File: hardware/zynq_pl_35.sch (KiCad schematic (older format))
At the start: 1 part

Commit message: Added a few Todos.
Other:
- note added: "TODO: VCCO(AFAIK 1,8 V), is VREF needed for this single ended signals?"
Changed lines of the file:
@@
 Wire Wire Line
 	5050 2400 5400 2400
+Text Notes 1000 850  0    60   ~ 0
+TODO: VCCO(AFAIK 1,8 V), is VREF needed for this single ended signals?
 $EndSCHEMATC

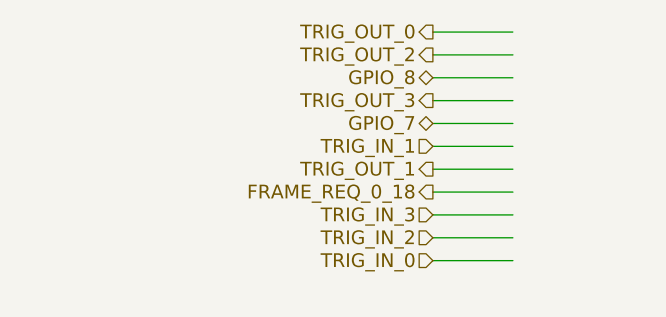
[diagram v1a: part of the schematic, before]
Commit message: Added decoupling Capacitors for the Zynq. Also added the 2,5 V Power supply.
The 2,5 V supply was implemented as LDO and is sourced by the 3,3 V Line.
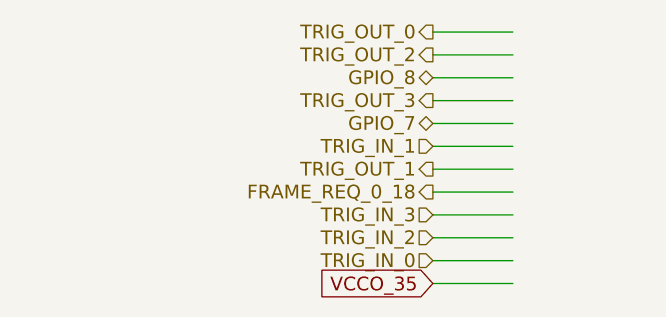
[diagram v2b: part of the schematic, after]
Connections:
- net labels added: VCCO_35
- wire segments 41 -> 42
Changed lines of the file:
@@
 Text Notes 1000 850  0    60   ~ 0
 TODO: VCCO(AFAIK 1,8 V), is VREF needed for this single ended signals?
+Text GLabel 5050 6400 0    60   Input ~ 0
+VCCO_35
+Wire Wire Line
+	5050 6400 5400 6400
 $EndSCHEMATC

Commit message: Started to route DDR3 Memory.
At first added missing Footprint for Reference- and Terminationvoltage Regulator. Added Powerplanes for GND and VCCO. Added decoupling Network to both DDR3 Memory Chips. There are more small caps, to support Memory from other Manufactors.
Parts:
- gave numbers to parts that had none: 1
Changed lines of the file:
@@
 $EndDescr
 $Comp
-L xc7z030sbg485 U?
+L xc7z030sbg485 U1
 U 4 1 596E7B8E
 P 5400 1400
-F 0 "U?" H 5600 1650 60  0000 L CNN
+F 0 "U1" H 5600 1650 60  0000 L CNN
 F 1 "xc7z030sbg485" H 5600 1550 60  0000 L CNN
 F 2 "footprints:SBG485_22x22_19.0x19.0mm_Pitch0.8mm" H 5400 1400 60  0001 C CNN

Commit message: Added Power/Protection Circuit
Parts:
- renumbered U1 to U201
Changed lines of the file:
@@
 $EndDescr
 $Comp
-L xc7z030sbg485 U1
+L xc7z030sbg485 U201
 U 4 1 596E7B8E
 P 5400 1400
-F 0 "U1" H 5600 1650 60  0000 L CNN
+F 0 "U201" H 5600 1650 60  0000 L CNN
 F 1 "xc7z030sbg485" H 5600 1550 60  0000 L CNN
 F 2 "footprints:SBG485_22x22_19.0x19.0mm_Pitch0.8mm" H 5400 1400 60  0001 C CNN
